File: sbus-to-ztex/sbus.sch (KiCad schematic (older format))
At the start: 14 parts, among them U1 SN74CB3T16211DGGR, U2 SN74CB3T16211DGGR, U3 SN74CB3T16211DGGR, U4 SN74CB3T3125PW

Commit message: Commit first go at v1.2
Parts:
- SBus1: URL (none) -> https://www2.mouser.com/ProductDetail/Fujitsu/FCN-234P096-G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
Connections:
- net SBUS_3V3_INT[4]*: now also R31.2, U_INT1.3
- net SBUS_3V3_INT[7]*: no longer R31.2, U_INT1.3
- net SBUS_5V_INT[4]*: now also U_INT1.4
- net SBUS_5V_INT[7]*: no longer U_INT1.4
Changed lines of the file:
@@
 $Descr A2 23386 16535
 encoding utf-8
-Sheet 2 5
+Sheet 2 6
 Title "sbus-to-ztex SBus connection & level shifting"
 Date ""
@@
 F 5 "817-FCN-234P096-G/Y " H 18450 3300 50  0001 C CNN "Mouser"
 F 6 "https://www2.mouser.com/ProductDetail/Fujitsu/FCN-234P096-G-Y?qs=uqct%252BzVq%2FBfM88%2F7KmJJ2Q%3D%3D" H 18450 3300 50  0001 C CNN "bom_link"
+F 7 "https://www2.mouser.com/ProductDetail/Fujitsu/FCN-234P096-G-Y?qs=%2Fha2pyFadugZ9WCm2lJ8CZdXc85UARoDXS81raJopvR1w4UDuaXlcQ%3D%3D" H 18450 3300 50  0001 C CNN "URL"
 	1    18450 3300
 	1    0    0    -1
 $EndComp
-Text GLabel 19000 7750 2    60   Input ~ 0
+Text GLabel 19000 6450 2    60   Input ~ 0
 SBUS_5V_INT[7]*
 Text GLabel 19200 5250 2    60   Input ~ 0
@@
 Text GLabel 19200 5350 2    60   Input ~ 0
 SBUS_5V_INT[5]*
-Text GLabel 19200 5450 2    60   Input ~ 0
+Text GLabel 19000 7750 2    60   Input ~ 0
 SBUS_5V_INT[4]*
 Text GLabel 19200 5550 2    60   Input ~ 0
@@
 Text GLabel 19000 7400 2    60   Input ~ 0
 SBUS_5V_INT[1]*
-Text GLabel 18050 7750 0    60   Input ~ 0
+Text GLabel 17850 6250 0    60   Input ~ 0
 SBUS_3V3_INT[7]*
 Text GLabel 18650 5250 0    60   Input ~ 0
@@
 Text GLabel 18650 5350 0    60   Input ~ 0
 SBUS_3V3_INT[5]*
-Text GLabel 18650 5450 0    60   Input ~ 0
+Text GLabel 18050 7750 0    60   Input ~ 0
 SBUS_3V3_INT[4]*
 Text GLabel 18650 5550 0    60   Input ~ 0

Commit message: fix footprints for SeeedStudio DRC results
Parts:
- U1, U2, U3: footprint Package_SO:TSSOP-56_6.1x14mm_P0.5mm -> For_SeeedStudio:TSSOP-56_6.1x14mm_P0.5mm_For_SeeedStudio
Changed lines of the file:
@@
 F 0 "U1" H 2750 2587 60  0000 C CNN
 F 1 "SN74CB3T16211DGGR" H 2750 2481 60  0000 C CNN
-F 2 "Package_SO:TSSOP-56_6.1x14mm_P0.5mm" H 2750 2440 60  0001 C CNN
+F 2 "For_SeeedStudio:TSSOP-56_6.1x14mm_P0.5mm_For_SeeedStudio" H 2750 2440 60  0001 C CNN
 F 3 "https://www.ti.com/lit/ds/symlink/sn74cb3t16211.pdf" H 1950 2200 60  0000 C CNN
 F 4 "SN74CB3T16211DGGR" H 1950 2200 50  0001 C CNN "MPN"
@@
 F 0 "U2" H 6550 2587 60  0000 C CNN
 F 1 "SN74CB3T16211DGGR" H 6550 2481 60  0000 C CNN
-F 2 "Package_SO:TSSOP-56_6.1x14mm_P0.5mm" H 6550 2440 60  0001 C CNN
+F 2 "For_SeeedStudio:TSSOP-56_6.1x14mm_P0.5mm_For_SeeedStudio" H 6550 2440 60  0001 C CNN
 F 3 "" H 5750 2200 60  0000 C CNN
 F 4 "SN74CB3T16211DGGR" H 5750 2200 50  0001 C CNN "MPN"
@@
 F 0 "U3" H 10350 2587 60  0000 C CNN
 F 1 "SN74CB3T16211DGGR" H 10350 2481 60  0000 C CNN
-F 2 "Package_SO:TSSOP-56_6.1x14mm_P0.5mm" H 10350 2440 60  0001 C CNN
+F 2 "For_SeeedStudio:TSSOP-56_6.1x14mm_P0.5mm_For_SeeedStudio" H 10350 2440 60  0001 C CNN
 F 3 "" H 9550 2200 60  0000 C CNN
 F 4 "SN74CB3T16211DGGR" H 9550 2200 50  0001 C CNN "MPN"

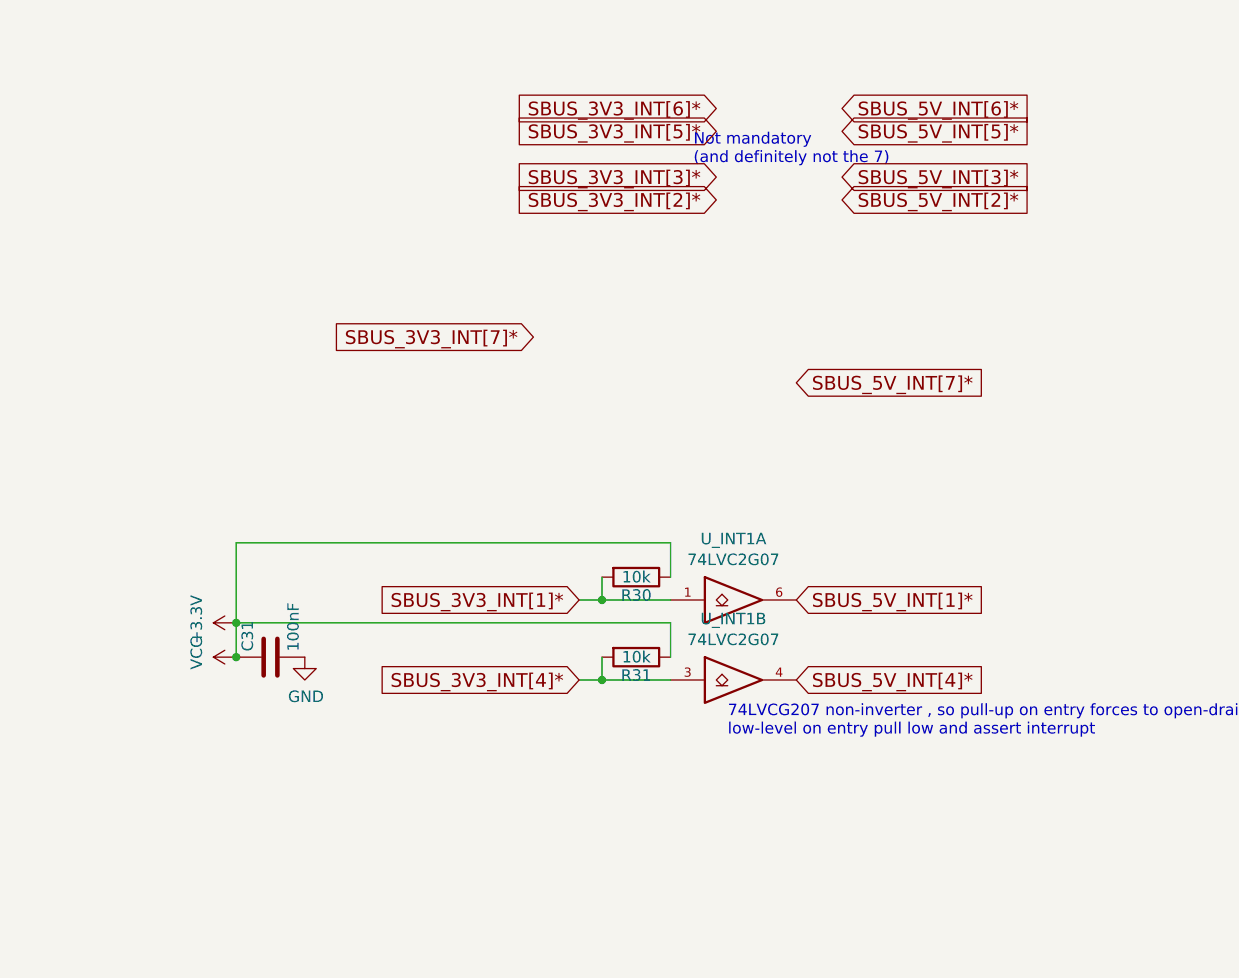
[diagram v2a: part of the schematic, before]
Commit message: update some MPN w/ SeeedStudio replacement
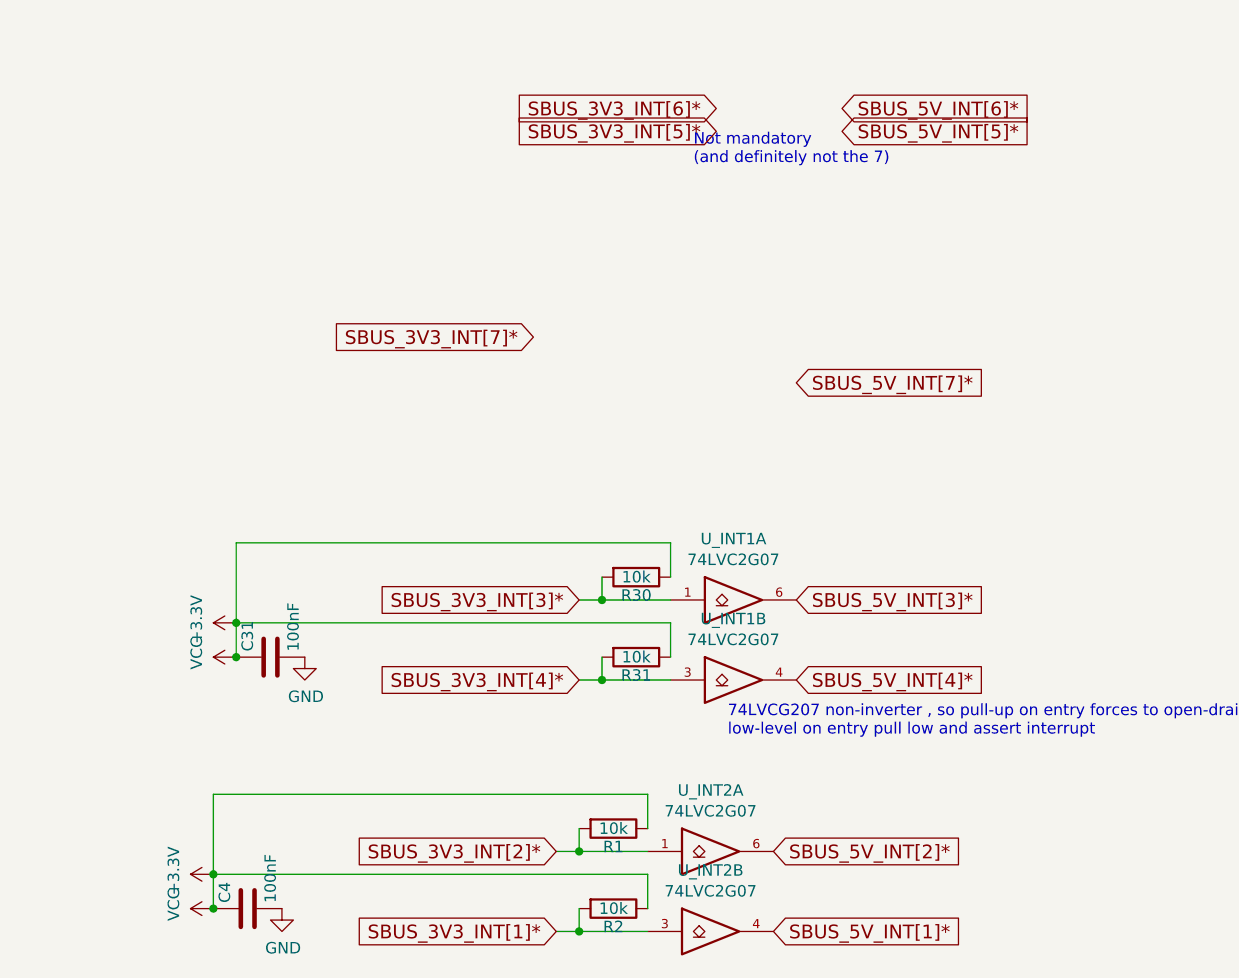
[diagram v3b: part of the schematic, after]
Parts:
- added C4: 100nF, Capacitor_SMD:C_0603_1608Metric, symbol Device:C
- added R1, R2: 10k, Resistor_SMD:R_0603_1608Metric, symbol Device:R
- added U_INT2: 74LVC2G07, Package_TO_SOT_SMD:SOT-23-6, symbol 74xGxx:74AUC2G07
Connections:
- net +3V3: now also C4.1, R1.1, R2.1, U_INT2.5 (VCC), U_INT2.5 (VCC)
- net GND: now also C4.2, U_INT2.2 (GND), U_INT2.2 (GND)
- net SBUS_3V3_INT[1]*: now also R2.2, U_INT2.3; no longer R30.2, U_INT1.1
- net SBUS_3V3_INT[2]*: now also R1.2, U_INT2.1
- net SBUS_3V3_INT[3]*: now also R30.2, U_INT1.1
- net SBUS_5V_INT[1]*: now also U_INT2.4; no longer U_INT1.6
- net SBUS_5V_INT[2]*: now also U_INT2.6
- net SBUS_5V_INT[3]*: now also U_INT1.6
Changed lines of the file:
@@
 Text GLabel 19000 7750 2    60   Input ~ 0
 SBUS_5V_INT[4]*
-Text GLabel 19200 5550 2    60   Input ~ 0
+Text GLabel 19000 7400 2    60   Input ~ 0
 SBUS_5V_INT[3]*
-Text GLabel 19200 5650 2    60   Input ~ 0
+Text GLabel 18900 8500 2    60   Input ~ 0
 SBUS_5V_INT[2]*
-Text GLabel 19000 7400 2    60   Input ~ 0
+Text GLabel 18900 8850 2    60   Input ~ 0
 SBUS_5V_INT[1]*
 Text GLabel 17850 6250 0    60   Input ~ 0
@@
 Text GLabel 18050 7750 0    60   Input ~ 0
 SBUS_3V3_INT[4]*
-Text GLabel 18650 5550 0    60   Input ~ 0
+Text GLabel 18050 7400 0    60   Input ~ 0
 SBUS_3V3_INT[3]*
-Text GLabel 18650 5650 0    60   Input ~ 0
+Text GLabel 17950 8500 0    60   Input ~ 0
 SBUS_3V3_INT[2]*
-Text GLabel 18050 7400 0    60   Input ~ 0
-SBUS_3V3_INT[1]*
 Text GLabel 11150 3100 2    60   Input ~ 0
 SBUS_5V_D[00]
@@
 Text Notes 500  5100 0    50   ~ 0
 BEWARE\nthe order\n(for routing)
+$Comp
+L power:VCC #PWR0131
+U 1 1 60DE3981
+P 16450 8750
+F 0 "#PWR0131" H 16450 8600 50  0001 C CNN
+F 1 "VCC" H 16467 8923 50  0000 C CNN
+F 2 "" H 16450 8750 50  0001 C CNN
+F 3 "" H 16450 8750 50  0001 C CNN
+	1    16450 8750
+	0    -1   -1   0
+$EndComp
+$Comp
+L power:+3.3V #PWR0132
+U 1 1 60DE3987
+P 16450 8600
+F 0 "#PWR0132" H 16450 8450 50  0001 C CNN
+F 1 "+3.3V" H 16465 8773 50  0000 C CNN
+F 2 "" H 16450 8600 50  0001 C CNN
+F 3 "" H 16450 8600 50  0001 C CNN
+	1    16450 8600
+	0    -1   -1   0
+$EndComp
+Wire Wire Line
+	16450 8600 16450 8750
+$Comp
+L power:GND #PWR0133
+U 1 1 60DE398E
+P 16750 8750
+F 0 "#PWR0133" H 16750 8500 50  0001 C CNN
+F 1 "GND" H 16755 8577 50  0000 C CNN
+F 2 "" H 16750 8750 50  0001 C CNN
+F 3 "" H 16750 8750 50  0001 C CNN
+	1    16750 8750
+	1    0    0    -1
+$EndComp
+$Comp
+L Device:C C4
+U 1 1 60DE399B
+P 16600 8750
+F 0 "C4" H 16625 8850 50  0000 L CNN
+F 1 "100nF" H 16625 8650 50  0000 L CNN
+F 2 "Capacitor_SMD:C_0603_1608Metric" H 16638 8600 50  0001 C CNN
+F 3 "" H 16600 8750 50  0000 C CNN
+F 4 "www.yageo.com" H 16600 8750 50  0001 C CNN "MNF1_URL"
+F 5 "CC0603KRX7R8BB104" H 16600 8750 50  0001 C CNN "MPN"
+F 6 "603-CC603KRX7R8BB104" H 16600 8750 50  0001 C CNN "Mouser"
+F 7 "?" H 16600 8750 50  0001 C CNN "Digikey"
+F 8 "?" H 16600 8750 50  0001 C CNN "LCSC"
+F 9 "?" H 16600 8750 50  0001 C CNN "Koncar"
+F 10 "TB" H 16600 8750 50  0001 C CNN "Side"
+	1    16600 8750
+	0    -1   -1   0
+$EndComp
+Connection ~ 16450 8750
+$Comp
+L Device:R R?
+U 1 1 60DE39A4
+P 18200 8400
+AR Path="/5F6B165A/60DE39A4" Ref="R?"  Part="1"
+AR Path="/5F679B53/60DE39A4" Ref="R1"  Part="1"
+F 0 "R1" V 18280 8400 50  0000 C CNN
+F 1 "10k" V 18200 8400 50  0000 C CNN
+F 2 "Resistor_SMD:R_0603_1608Metric" V 18130 8400 50  0001 C CNN
+F 3 "" H 18200 8400 50  0000 C CNN
+F 4 "0603WAF1002T5E" V 18200 7800 50  0001 C CNN "MPN"
+	1    18200 8400
+	0    1    1    0
+$EndComp
+$Comp
+L Device:R R?
+U 1 1 60DE39AC
+P 18200 8750
+AR Path="/5F6B165A/60DE39AC" Ref="R?"  Part="1"
+AR Path="/5F679B53/60DE39AC" Ref="R2"  Part="1"
+F 0 "R2" V 18280 8750 50  0000 C CNN
+F 1 "10k" V 18200 8750 50  0000 C CNN
+F 2 "Resistor_SMD:R_0603_1608Metric" V 18130 8750 50  0001 C CNN
+F 3 "" H 18200 8750 50  0000 C CNN
+F 4 "0603WAF1002T5E" V 18200 8150 50  0001 C CNN "MPN"
+	1    18200 8750
+	0    1    1    0
+$EndComp
+Wire Wire Line
+	17950 8850 18050 8850
+Wire Wire Line
+	17950 8500 18050 8500
+Wire Wire Line
+	18050 8400 18050 8500
+Connection ~ 18050 8500
+Wire Wire Line
+	18050 8500 18350 8500
+Wire Wire Line
+	18050 8750 18050 8850
+Connection ~ 18050 8850
+Wire Wire Line
+	18050 8850 18350 8850
+Wire Wire Line
+	16450 8600 18350 8600
+Wire Wire Line
+	18350 8600 18350 8750
+Connection ~ 16450 8600
+Wire Wire Line
+	18350 8400 18350 8250
+Wire Wire Line
+	18350 8250 16450 8250
+Wire Wire Line
+	16450 8250 16450 8600
+$Comp
+L 74xGxx:74AUC2G07 U_INT2
+U 1 1 60DE39C3
+P 18650 8500
+F 0 "U_INT2" H 18625 8767 50  0000 C CNN
+F 1 "74LVC2G07" H 18625 8676 50  0000 C CNN
+F 2 "Package_TO_SOT_SMD:SOT-23-6" H 18650 8500 50  0001 C CNN
+F 3 "https://www.diodes.com/assets/Datasheets/74LVC2G07.pdf" H 18650 8500 50  0001 C CNN
+F 4 "SN74LVC2G07DBVR" H 18650 8500 50  0001 C CNN "MPN"
+	1    18650 8500
+	1    0    0    -1
+$EndComp
+$Comp
+L 74xGxx:74AUC2G07 U_INT2
+U 2 1 60DE39CA
+P 18650 8850
+F 0 "U_INT2" H 18625 9117 50  0000 C CNN
+F 1 "74LVC2G07" H 18625 9026 50  0000 C CNN
+F 2 "" H 18650 8850 50  0001 C CNN
+F 3 "http://www.ti.com/lit/sg/scyt129e/scyt129e.pdf" H 18650 8850 50  0001 C CNN
+	2    18650 8850
+	1    0    0    -1
+$EndComp
+Text GLabel 17950 8850 0    60   Input ~ 0
+SBUS_3V3_INT[1]*
 $EndSCHEMATC

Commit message: Fewer LEDs, more interrupts, replace USB VBus power chip by something that might be available..., update signals file
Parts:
- added C7, C8: 100nF, Capacitor_SMD:C_0603_1608Metric, symbol Device:C
- added R5, R6: 10k, Resistor_SMD:R_0603_1608Metric, symbol Device:R
- added U_INT3: 74LVC2G07, Package_TO_SOT_SMD:SOT-23-6, symbol 74xGxx:74AUC2G07
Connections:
- net +3V3: now also C7.1, C8.1, R5.1, R6.1, U_INT3.5 (VCC), U_INT3.5 (VCC)
- net GND: now also C7.2, C8.2, U_INT3.2 (GND), U_INT3.2 (GND)
- net SBUS_3V3_INT[5]*: now also R6.2, U_INT3.3
- net SBUS_3V3_INT[6]*: now also R5.2, U_INT3.1
- net SBUS_5V_INT[5]*: now also U_INT3.4
- net SBUS_5V_INT[6]*: now also U_INT3.6
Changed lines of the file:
@@
 Text GLabel 19000 6450 2    60   Input ~ 0
 SBUS_5V_INT[7]*
-Text GLabel 19200 5250 2    60   Input ~ 0
+Text GLabel 18900 9650 2    60   Input ~ 0
 SBUS_5V_INT[6]*
-Text GLabel 19200 5350 2    60   Input ~ 0
+Text GLabel 18900 10000 2    60   Input ~ 0
 SBUS_5V_INT[5]*
 Text GLabel 19000 7750 2    60   Input ~ 0
@@
 Text GLabel 17850 6250 0    60   Input ~ 0
 SBUS_3V3_INT[7]*
-Text GLabel 18650 5250 0    60   Input ~ 0
+Text GLabel 17950 9650 0    60   Input ~ 0
 SBUS_3V3_INT[6]*
-Text GLabel 18650 5350 0    60   Input ~ 0
+Text GLabel 17950 10000 0    60   Input ~ 0
 SBUS_3V3_INT[5]*
 Text GLabel 18050 7750 0    60   Input ~ 0
@@
 Text GLabel 17950 8850 0    60   Input ~ 0
 SBUS_3V3_INT[1]*
+$Comp
+L power:VCC #PWR0139
+U 1 1 612A613B
+P 16450 9900
+F 0 "#PWR0139" H 16450 9750 50  0001 C CNN
+F 1 "VCC" H 16467 10073 50  0000 C CNN
+F 2 "" H 16450 9900 50  0001 C CNN
+F 3 "" H 16450 9900 50  0001 C CNN
+	1    16450 9900
+	0    -1   -1   0
+$EndComp
+$Comp
+L power:+3.3V #PWR0140
+U 1 1 612A6141
+P 16450 9750
+F 0 "#PWR0140" H 16450 9600 50  0001 C CNN
+F 1 "+3.3V" H 16465 9923 50  0000 C CNN
+F 2 "" H 16450 9750 50  0001 C CNN
+F 3 "" H 16450 9750 50  0001 C CNN
+	1    16450 9750
+	0    -1   -1   0
+$EndComp
+Wire Wire Line
+	16450 9750 16450 9900
+$Comp
+L power:GND #PWR0141
+U 1 1 612A6148
+P 16750 9900
+F 0 "#PWR0141" H 16750 9650 50  0001 C CNN
+F 1 "GND" H 16755 9727 50  0000 C CNN
+F 2 "" H 16750 9900 50  0001 C CNN
+F 3 "" H 16750 9900 50  0001 C CNN
+	1    16750 9900
+	1    0    0    -1
+$EndComp
+$Comp
+L Device:C C7
+U 1 1 612A6155
+P 16600 9900
+F 0 "C7" H 16625 10000 50  0000 L CNN
+F 1 "100nF" H 16625 9800 50  0000 L CNN
+F 2 "Capacitor_SMD:C_0603_1608Metric" H 16638 9750 50  0001 C CNN
+F 3 "" H 16600 9900 50  0000 C CNN
+F 4 "www.yageo.com" H 16600 9900 50  0001 C CNN "MNF1_URL"
+F 5 "CC0603KRX7R8BB104" H 16600 9900 50  0001 C CNN "MPN"
+F 6 "603-CC603KRX7R8BB104" H 16600 9900 50  0001 C CNN "Mouser"
+F 7 "?" H 16600 9900 50  0001 C CNN "Digikey"
+F 8 "?" H 16600 9900 50  0001 C CNN "LCSC"
+F 9 "?" H 16600 9900 50  0001 C CNN "Koncar"
+F 10 "TB" H 16600 9900 50  0001 C CNN "Side"
+	1    16600 9900
+	0    -1   -1   0
+$EndComp
+Connection ~ 16450 9900
+$Comp
+L Device:R R?
+U 1 1 612A615E
+P 18200 9550
+AR Path="/5F6B165A/612A615E" Ref="R?"  Part="1"
+AR Path="/5F679B53/612A615E" Ref="R5"  Part="1"
+F 0 "R5" V 18280 9550 50  0000 C CNN
+F 1 "10k" V 18200 9550 50  0000 C CNN
+F 2 "Resistor_SMD:R_0603_1608Metric" V 18130 9550 50  0001 C CNN
+F 3 "" H 18200 9550 50  0000 C CNN
+F 4 "0603WAF1002T5E" V 18200 8950 50  0001 C CNN "MPN"
+	1    18200 9550
+	0    1    1    0
+$EndComp
+$Comp
+L Device:R R?
+U 1 1 612A6166
+P 18200 9900
+AR Path="/5F6B165A/612A6166" Ref="R?"  Part="1"
+AR Path="/5F679B53/612A6166" Ref="R6"  Part="1"
+F 0 "R6" V 18280 9900 50  0000 C CNN
+F 1 "10k" V 18200 9900 50  0000 C CNN
+F 2 "Resistor_SMD:R_0603_1608Metric" V 18130 9900 50  0001 C CNN
+F 3 "" H 18200 9900 50  0000 C CNN
+F 4 "0603WAF1002T5E" V 18200 9300 50  0001 C CNN "MPN"
+	1    18200 9900
+	0    1    1    0
+$EndComp
+Wire Wire Line
+	17950 10000 18050 10000
+Wire Wire Line
+	17950 9650 18050 9650
+Wire Wire Line
+	18050 9550 18050 9650
+Connection ~ 18050 9650
+Wire Wire Line
+	18050 9650 18350 9650
+Wire Wire Line
+	18050 9900 18050 10000
+Connection ~ 18050 10000
+Wire Wire Line
+	18050 10000 18350 10000
+Wire Wire Line
+	16450 9750 18350 9750
+Wire Wire Line
+	18350 9750 18350 9900
+Connection ~ 16450 9750
+Wire Wire Line
+	18350 9550 18350 9400
+Wire Wire Line
+	18350 9400 16450 9400
+Wire Wire Line
+	16450 9400 16450 9750
+$Comp
+L 74xGxx:74AUC2G07 U_INT3
+U 1 1 612A617C
+P 18650 9650
+F 0 "U_INT3" H 18625 9917 50  0000 C CNN
+F 1 "74LVC2G07" H 18625 9826 50  0000 C CNN
+F 2 "Package_TO_SOT_SMD:SOT-23-6" H 18650 9650 50  0001 C CNN
+F 3 "https://www.diodes.com/assets/Datasheets/74LVC2G07.pdf" H 18650 9650 50  0001 C CNN
+F 4 "SN74LVC2G07DBVR" H 18650 9650 50  0001 C CNN "MPN"
+	1    18650 9650
+	1    0    0    -1
+$EndComp
+$Comp
+L 74xGxx:74AUC2G07 U_INT3
+U 2 1 612A6183
+P 18650 10000
+F 0 "U_INT3" H 18625 10267 50  0000 C CNN
+F 1 "74LVC2G07" H 18625 10176 50  0000 C CNN
+F 2 "" H 18650 10000 50  0001 C CNN
+F 3 "http://www.ti.com/lit/sg/scyt129e/scyt129e.pdf" H 18650 10000 50  0001 C CNN
+	2    18650 10000
+	1    0    0    -1
+$EndComp
+$Comp
+L Device:C C8
+U 1 1 612BD908
+P 6600 9200
+F 0 "C8" H 6625 9300 50  0000 L CNN
+F 1 "100nF" H 6625 9100 50  0000 L CNN
+F 2 "Capacitor_SMD:C_0603_1608Metric" H 6638 9050 50  0001 C CNN
+F 3 "" H 6600 9200 50  0000 C CNN
+F 4 "www.yageo.com" H 6600 9200 50  0001 C CNN "MNF1_URL"
+F 5 "CC0603KRX7R8BB104" H 6600 9200 50  0001 C CNN "MPN"
+F 6 "603-CC603KRX7R8BB104" H 6600 9200 50  0001 C CNN "Mouser"
+F 7 "?" H 6600 9200 50  0001 C CNN "Digikey"
+F 8 "?" H 6600 9200 50  0001 C CNN "LCSC"
+F 9 "?" H 6600 9200 50  0001 C CNN "Koncar"
+F 10 "TB" H 6600 9200 50  0001 C CNN "Side"
+	1    6600 9200
+	1    0    0    -1
+$EndComp
+$Comp
+L power:GND #PWR0142
+U 1 1 612BD90F
+P 6600 9350
+F 0 "#PWR0142" H 6600 9100 50  0001 C CNN
+F 1 "GND" H 6605 9177 50  0000 C CNN
+F 2 "" H 6600 9350 50  0001 C CNN
+F 3 "" H 6600 9350 50  0001 C CNN
+	1    6600 9350
+	1    0    0    -1
+$EndComp
+$Comp
+L power:+3.3V #PWR0143
+U 1 1 612C0425
+P 6600 9050
+F 0 "#PWR0143" H 6600 8900 50  0001 C CNN
+F 1 "+3.3V" H 6615 9223 50  0000 C CNN
+F 2 "" H 6600 9050 50  0001 C CNN
+F 3 "" H 6600 9050 50  0001 C CNN
+	1    6600 9050
+	1    0    0    -1
+$EndComp
 $EndSCHEMATC

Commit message: Update more stuff to V1.2
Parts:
- U3: URL (none) -> https://lcsc.com/product-detail/Signal-Switches-Encoders-De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; URL-alt (none) -> https://www.mouser.fr/ProductDetail/Texas-Instruments/SN74C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
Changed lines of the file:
@@
 F 3 "" H 9550 2200 60  0000 C CNN
 F 4 "SN74CB3T16211DGGR" H 9550 2200 50  0001 C CNN "MPN"
+F 5 "https://www.mouser.fr/ProductDetail/Texas-Instruments/SN74CB3T16211DGGR?qs=%2Fha2pyFadujLgV8PJqueL5aUGpX9%252BbECTuUAq6EU8VAiPml4qcD9lw%3D%3D" H 9550 2200 50  0001 C CNN "URL-alt"
+F 6 "https://lcsc.com/product-detail/Signal-Switches-Encoders-Decoders-Multiplexers_Texas-Instruments-SN74CB3T16211DGGR_C2653275.html" H 9550 2200 50  0001 C CNN "URL"
 	1    9550 2200
 	1    0    0    -1
